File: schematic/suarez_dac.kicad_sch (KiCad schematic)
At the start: 26 parts, among them M1 1 / 0.15 um, M10 2 / 0.35 um LVT, M11 1 / 0.15 um, M12 2 / 0.35 um LVT, M13 4 / 2 um, M14 4 / 2 um, M15 4 / 1 um LVT, M16 4 / 1 um LVT, M17 4 / 2 um, M18 4 / 2 um, M19 24 / 2 um, M2 2 / 0.15 um, M20 20 / 1 um, M3 1 / 0.15 um, M4 2 / 0.15 um, M5 1 / 0.15 um, M6 2 / 0.15 um, M7 1 / 0.15 um, M8 2 / 0.35 um LVT, M9 1 / 0.15 um

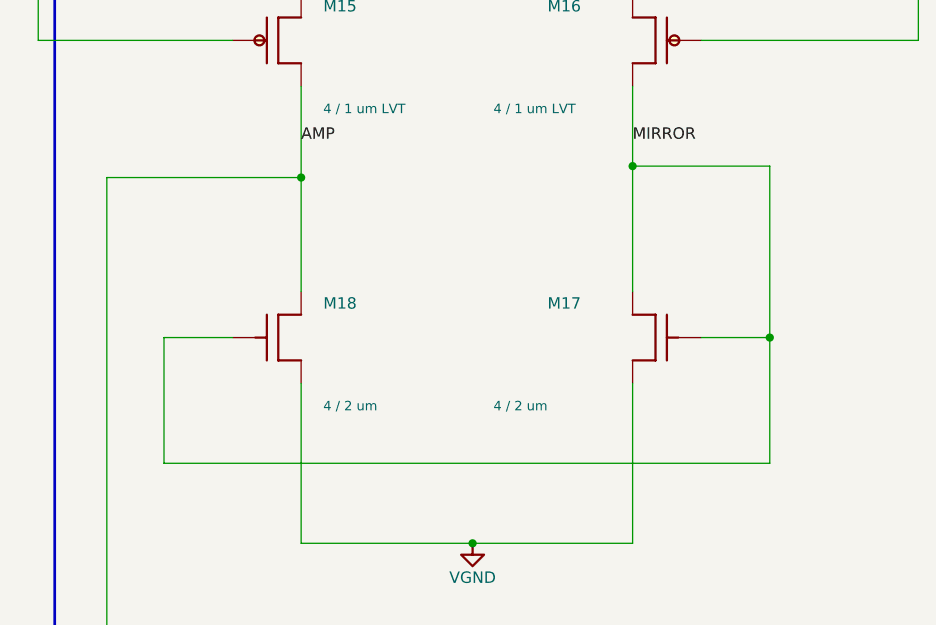
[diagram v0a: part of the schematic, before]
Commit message: Redraw buffer current mirror in conventional schematic form
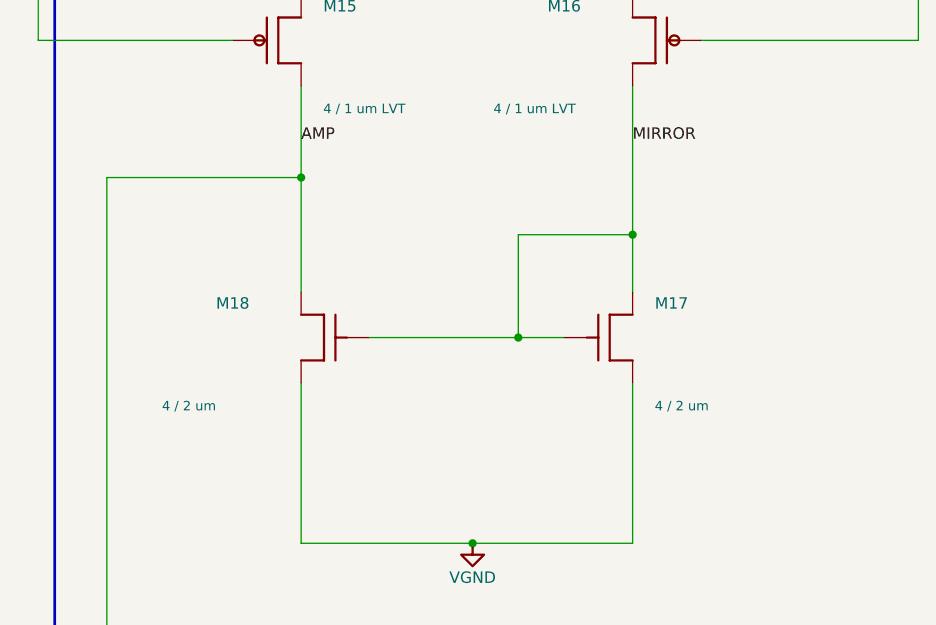
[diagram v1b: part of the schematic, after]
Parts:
- removed M17: 4 / 2 um, symbol Sky130:NMOS_R3
- removed M18: 4 / 2 um, symbol Sky130:NMOS3
- added M17: 4 / 2 um, symbol Sky130:NMOS3
- added M18: 4 / 2 um, symbol Sky130:NMOS_R3
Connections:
- net AMP: now also M18.1 (D)
- net MIRROR: now also M17.1 (D), M17.2 (G), M18.2 (G)
- net VGND: now also M17.3 (S), M18.3 (S)
